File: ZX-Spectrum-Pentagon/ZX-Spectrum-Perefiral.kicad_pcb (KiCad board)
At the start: 2 copper layers, 4 parts, among them U1 74HC00

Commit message: add zxm_extrime_extension add 74XX283 to 74IEC start ZX-Spectrum-Perefiral project
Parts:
- removed C1: C, Capacitor_SMD:C_0805_2012Metric_Pad1.18x1.45mm_HandSolder
- removed R1, R2: R, Resistor_SMD:R_0805_2012Metric_Pad1.20x1.40mm_HandSolder
- removed U1: 74HC00, Package_SO:SOIC-14_3.9x8.7mm_P1.27mm
- added H1: MountingHole_Pad, MountingHole:MountingHole_3.2mm_M3_Pad_Via, F.Cu at (127.0, 24.1)
- added H2: MountingHole_Pad, MountingHole:MountingHole_3.2mm_M3_Pad_Via, F.Cu at (215.9, 39.4)
- added H3: MountingHole_Pad, MountingHole:MountingHole_3.2mm_M3_Pad_Via, F.Cu at (228.6, 64.8)
- added H4: MountingHole_Pad, MountingHole:MountingHole_3.2mm_M3_Pad_Via, F.Cu at (228.6, 144.8)
- added H5: MountingHole_Pad, MountingHole:MountingHole_3.2mm_M3_Pad_Via, F.Cu at (24.1, 144.8)
- added H6: MountingHole_Pad, MountingHole:MountingHole_3.2mm_M3_Pad_Via, F.Cu at (24.1, 64.8)
- added JCPU1: TOP LEVEL, ZX-Spectrum-Pentagon:PinSocket_2x30_P2.54mm_Vertical, F.Cu at (174.0, 33.0)
- added XMCPU1: EDGE-28M5, ZX-Spectrum-Pentagon:EDGE_28M5-2.54, F.Cu at (172.4, 24.1)
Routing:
- added copper zone on F.Cu, net GND
- added copper zone on B.Cu, net VCC
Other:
- board outline added: 213.1 x 129 mm
- board text added: "EDGE connector position X=172.44 Y=24.13 BOARD connector position X=173.99 Y=33.02 Hole1: X=127 Y=24.13, Hole2: X=215.9 Y=39.37 Hole3: X=228.6 Y=64.77, Hole4: X=228.6 Y=144.78 Hole5: X=24.13 Y=144.78, Hole6: X=24.13 Y=64.77"

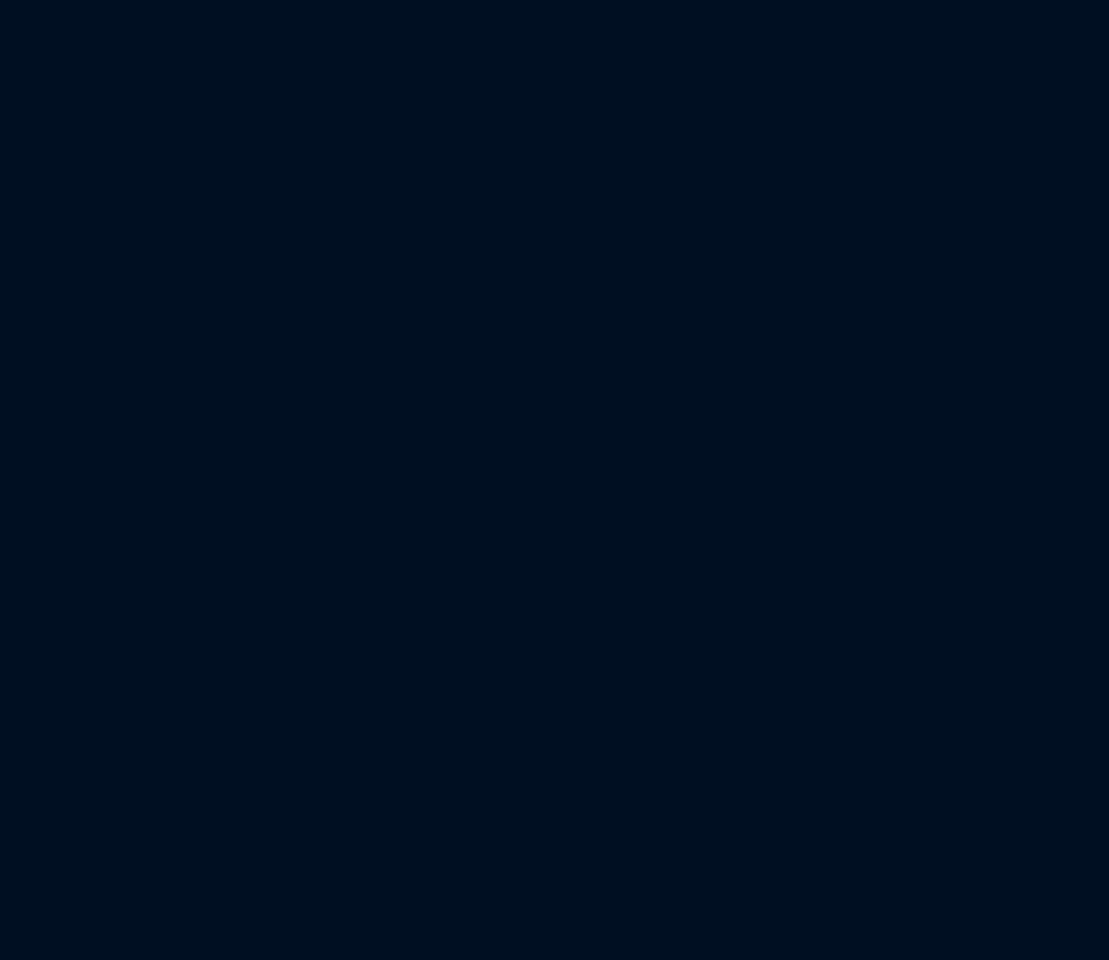
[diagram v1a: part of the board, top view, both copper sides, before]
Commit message: fix 74ICE, FDControlers, edge_lib library update all schematic and board fix ERC ZX-Spectrum-Perefiral
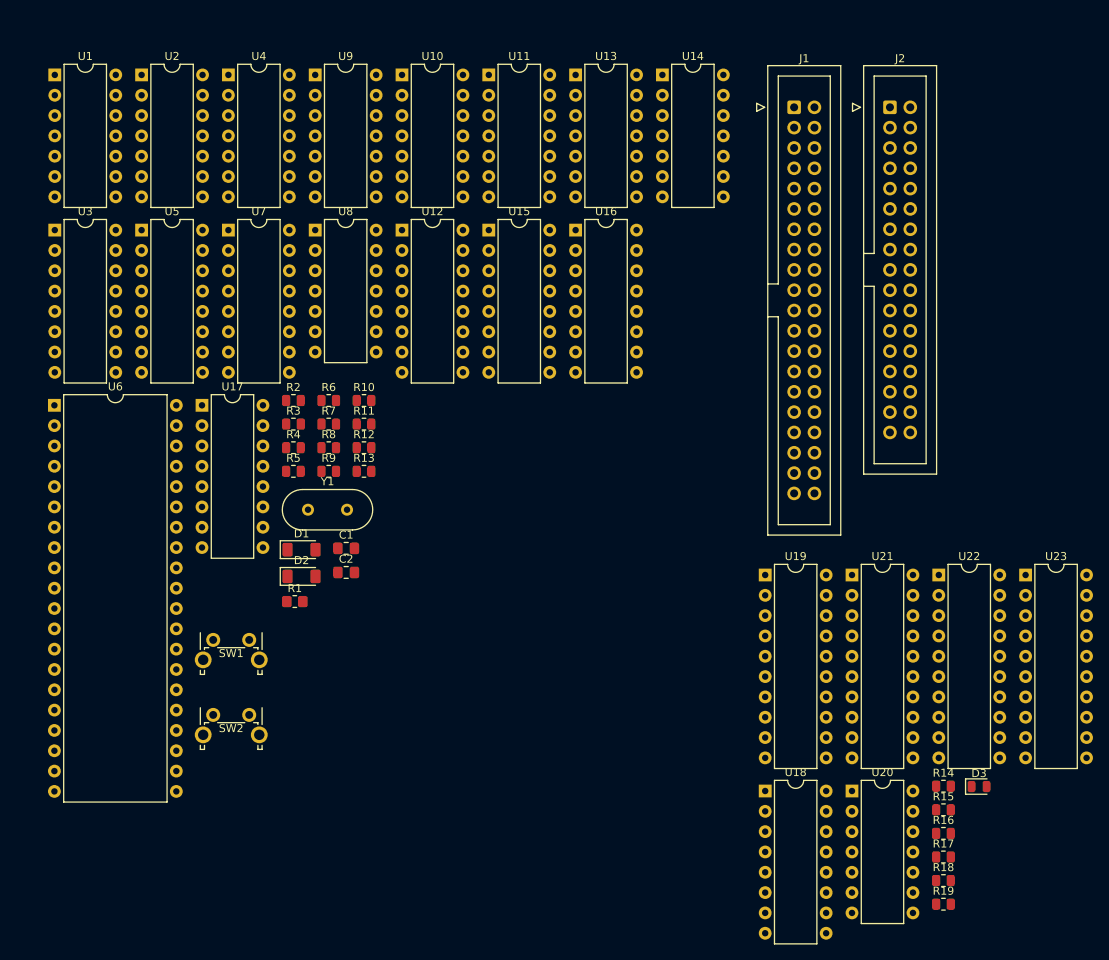
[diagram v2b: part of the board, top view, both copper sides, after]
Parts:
- added C1: 20pF, Capacitor_SMD:C_0805_2012Metric_Pad1.18x1.45mm_HandSolder, F.Cu at (284.6, 116.0)
- added C2: 20pF, Capacitor_SMD:C_0805_2012Metric_Pad1.18x1.45mm_HandSolder, F.Cu at (284.6, 119.1)
- added D1: 1N4148, Diode_SMD:D_MiniMELF, F.Cu at (279.1, 116.2)
- added D2: 1N4148, Diode_SMD:D_MiniMELF, F.Cu at (279.1, 119.6)
- added D3: RED, Diode_SMD:D_0805_2012Metric, F.Cu at (363.8, 145.8)
- added J1: IDE, Connector_IDC:IDC-Header_2x20_P2.54mm_Vertical, F.Cu at (340.6, 60.9)
- added J2: FDD, Connector_IDC:IDC-Header_2x17_P2.54mm_Vertical, F.Cu at (352.6, 60.9)
- added R1: 2MOm, Resistor_SMD:R_0805_2012Metric_Pad1.20x1.40mm_HandSolder, F.Cu at (278.2, 122.7)
- added R10: 10kOm, Resistor_SMD:R_0805_2012Metric, F.Cu at (286.9, 97.6)
- added R11: 10kOm, Resistor_SMD:R_0805_2012Metric, F.Cu at (286.9, 100.5)
- added R12: 10kOm, Resistor_SMD:R_0805_2012Metric, F.Cu at (286.9, 103.5)
- added R13: 10kOm, Resistor_SMD:R_0805_2012Metric, F.Cu at (286.9, 106.4)
- added R14: 10kOm, Resistor_SMD:R_0805_2012Metric, F.Cu at (359.3, 145.8)
- added R15: 10kOm, Resistor_SMD:R_0805_2012Metric, F.Cu at (359.3, 148.7)
- added R16: 10kOm, Resistor_SMD:R_0805_2012Metric, F.Cu at (359.3, 151.7)
- added R17: 10kOm, Resistor_SMD:R_0805_2012Metric, F.Cu at (359.3, 154.6)
- added R18: 10kOm, Resistor_SMD:R_0805_2012Metric, F.Cu at (359.3, 157.6)
- added R19: 10kOm, Resistor_SMD:R_0805_2012Metric, F.Cu at (359.3, 160.5)
- added R2: 10kOm, Resistor_SMD:R_0805_2012Metric, F.Cu at (278.1, 97.6)
- added R3: 10kOm, Resistor_SMD:R_0805_2012Metric, F.Cu at (278.1, 100.5)
- added R4: 1kOm, Resistor_SMD:R_0805_2012Metric, F.Cu at (278.1, 103.5)
- added R5: 1kOm, Resistor_SMD:R_0805_2012Metric, F.Cu at (278.1, 106.4)
- added R6: 1kOM, Resistor_SMD:R_0805_2012Metric, F.Cu at (282.5, 97.6)
- added R7: 1kOM, Resistor_SMD:R_0805_2012Metric, F.Cu at (282.5, 100.5)
- added R8: 1kOM, Resistor_SMD:R_0805_2012Metric, F.Cu at (282.5, 103.5)
- added R9: 10kOM, Resistor_SMD:R_0805_2012Metric, F.Cu at (282.5, 106.4)
- added SW1: MAGIC, Button_Switch_THT:SW_Tactile_SPST_Angled_PTS645Vx39-2LFS, F.Cu at (268.0, 127.5)
- added SW2: SOS/~{DOS}, Button_Switch_THT:SW_Tactile_SPST_Angled_PTS645Vx39-2LFS, F.Cu at (268.0, 136.9)
- added U1: 74HC04, Package_DIP:DIP-14_W7.62mm, F.Cu at (248.2, 56.9)
- added U10: 74HC03, Package_DIP:DIP-14_W7.62mm, F.Cu at (291.6, 56.9)
- added U11: 74HC74, Package_DIP:DIP-14_W7.62mm, F.Cu at (302.5, 56.9)
- added U12: 74HC166, Package_DIP:DIP-16_W7.62mm, F.Cu at (291.6, 76.3)
- added U13: 74HC30, Package_DIP:DIP-14_W7.62mm, F.Cu at (313.3, 56.9)
- added U14: 74HC32, Package_DIP:DIP-14_W7.62mm, F.Cu at (324.2, 56.9)
- added U15: 74HC175, Package_DIP:DIP-16_W7.62mm, F.Cu at (302.5, 76.3)
- added U16: 74HC161, Package_DIP:DIP-16_W7.62mm, F.Cu at (313.3, 76.3)
- added U17: 74HC283, Package_DIP:DIP-16_W7.62mm, F.Cu at (266.6, 98.2)
- added U18: 74HC138, Package_DIP:DIP-16_W7.62mm, F.Cu at (337.0, 146.4)
- added U19: 74HC245, Package_DIP:DIP-20_W7.62mm, F.Cu at (337.0, 119.4)
- added U2: 74HC74, Package_DIP:DIP-14_W7.62mm, F.Cu at (259.1, 56.9)
- added U20: 74HC32, Package_DIP:DIP-14_W7.62mm, F.Cu at (347.9, 146.4)
- added U21: 74HC574, Package_DIP:DIP-20_W7.62mm, F.Cu at (347.9, 119.4)
- added U22: 74HC244, Package_DIP:DIP-20_W7.62mm, F.Cu at (358.7, 119.4)
- added U23: 74HC574, Package_DIP:DIP-20_W7.62mm, F.Cu at (369.6, 119.4)
- added U3: 74HC138, Package_DIP:DIP-16_W7.62mm, F.Cu at (248.2, 76.3)
- added U4: 74HC05, Package_DIP:DIP-14_W7.62mm, F.Cu at (269.9, 56.9)
- added U5: 74HC367, Package_DIP:DIP-16_W7.62mm, F.Cu at (259.1, 76.3)
- added U6: FD1793, Package_DIP:DIP-40_W15.24mm, F.Cu at (248.2, 98.2)
- added U7: 74HC175, Package_DIP:DIP-16_W7.62mm, F.Cu at (269.9, 76.3)
- added U8: 74HC00, Package_DIP:DIP-14_W7.62mm, F.Cu at (280.8, 76.3)
- added U9: 74HC27, Package_DIP:DIP-14_W7.62mm, F.Cu at (280.8, 56.9)
- added Y1: 16MHz, Crystal:Crystal_HC49-U_Vertical, F.Cu at (279.9, 111.2)
- XMCPU1: footprint ZX-Spectrum-Pentagon:EDGE_28M5-2.54 -> edge:EDGE_28M5-2.54
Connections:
- net /Connectors/A0 renamed /A0
- net /Connectors/A1 renamed /A1
- net /Connectors/A10 renamed /A10
- net /Connectors/A11 renamed /A11
- net /Connectors/A12 renamed /A12
- net /Connectors/A13 renamed /A13
- net /Connectors/A14 renamed /A14
- net /Connectors/A15 renamed /A15
- net /Connectors/A2 renamed /A2
- net /Connectors/A3 renamed /A3
- net /Connectors/A4 renamed /A4
- net /Connectors/A5 renamed /A5
- net /Connectors/A6 renamed /A6
- net /Connectors/A7 renamed /A7
- net /Connectors/A8 renamed /A8
- net /Connectors/A9 renamed /A9
- net /Connectors/D0 renamed /D0
- net /Connectors/D1 renamed /D1
- net /Connectors/D2 renamed /D2
- net /Connectors/D3 renamed /D3
- net /Connectors/D4 renamed /D4
- net /Connectors/D5 renamed /D5
- net /Connectors/D6 renamed /D6
- net /Connectors/D7 renamed /D7
- net /Connectors/RA15 renamed /~{DOS}
- net /Connectors/~{IORQ} renamed /~{IORQ}
- net /Connectors/~{M1} renamed /~{M1}
- net /Connectors/~{MREQ} renamed /~{MREQ}
- net /Connectors/~{NMI} renamed /~{NMI}
- net /Connectors/~{RD} renamed /~{RD}
- net /Connectors/~{RESET} renamed /~{RESET}
- net /Connectors/~{WR} renamed /~{WR}
- JCPU1 pad 31: unconnected-(JCPU1-Pin_31-Pad31) -> /~{ZX128}
- XMCPU1 pad A16: unconnected-(XMCPU1-PadA16) -> /~{ZX128}

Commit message: FDControlers rename from VCC1 to VDD zx_custom_symbol add connector Conn_02x32_Odd_Even ZX-Spectrum-Pentagon rename from +9V to POWER ZX-Spectrum-Perefiral improve schematic
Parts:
- removed the D1 at (279.1, 116.2)
- removed JCPU1: TOP LEVEL, ZX-Spectrum-Pentagon:PinSocket_2x30_P2.54mm_Vertical
- added CPS1: 47uF/16V, Capacitor_Tantalum_SMD:CP_EIA-3216-18_Kemet-A_Pad1.58x1.35mm_HandSolder, F.Cu at (370.7, -26.0)
- added CPS2: 330uF/50V, Capacitor_Tantalum_SMD:CP_EIA-7343-31_Kemet-D_Pad2.25x2.55mm_HandSolder, F.Cu at (364.3, -36.4)
- added CPS3: 100nF, Capacitor_SMD:C_0805_2012Metric_Pad1.18x1.45mm_HandSolder, F.Cu at (371.8, -37.8)
- added CPS4: 330uF/50V, Capacitor_Tantalum_SMD:CP_EIA-7343-31_Kemet-D_Pad2.25x2.55mm_HandSolder, F.Cu at (364.3, -30.5)
- added CPS5: 100nF, Capacitor_SMD:C_0805_2012Metric_Pad1.18x1.45mm_HandSolder, F.Cu at (371.8, -34.8)
- added CPS6: 4,7uF/16V, Capacitor_Tantalum_SMD:CP_EIA-3216-18_Kemet-A_Pad1.58x1.35mm_HandSolder, F.Cu at (370.7, -22.9)
- added CPS7: 330pF, Capacitor_SMD:C_0805_2012Metric_Pad1.18x1.45mm_HandSolder, F.Cu at (371.8, -31.8)
- added D3: 1N4148, Diode_SMD:D_MiniMELF, F.Cu at (282.3, 131.2)
- added DPS1: 1N5819, Diode_SMD:D_SOD-323_HandSoldering, F.Cu at (347.0, -23.6)
- added DPS2: SS34, Diode_SMD:D_SMA, F.Cu at (370.9, -42.5)
- added J1: Conn_02x32_Odd_Even, Connector_PinSocket_2.54mm:PinSocket_2x32_P2.54mm_Vertical, F.Cu at (132.1, 31.8)
- added LPS1: 33uH, Inductor_SMD:L_12x12mm_H6mm, F.Cu at (351.8, -32.2)
- added LPS2: 220uH, CDInductor:CD43, F.Cu at (370.0, -48.2)
- added RPS1: 1, Resistor_SMD:R_0805_2012Metric_Pad1.20x1.40mm_HandSolder, F.Cu at (364.5, -50.2)
- added RPS2: 13kOm, Resistor_SMD:R_0805_2012Metric_Pad1.20x1.40mm_HandSolder, F.Cu at (364.5, -47.2)
- added RPS3: 180, Resistor_SMD:R_0805_2012Metric_Pad1.20x1.40mm_HandSolder, F.Cu at (364.5, -44.3)
- added RPS4: 1,5kOm, Resistor_SMD:R_0805_2012Metric_Pad1.20x1.40mm_HandSolder, F.Cu at (364.5, -41.3)
- added UPS1: LM2596S-5.0V, Package_TO_SOT_SMD:TO-263-5_TabPin3, F.Cu at (355.1, -45.5)
- added UPS2: MC34063A, Package_SO:SO-8_3.9x4.9mm_P1.27mm, F.Cu at (363.4, -24.2)
- SW2: value SOS/~{DOS} -> ~{SOS}/DOS
- moved D2 8.92 mm to (282.3, 127.9)
- moved U14 5.39 mm to (318.8, 56.9)
- moved U16 4.71 mm to (308.6, 76.2)
- moved U13 4.71 mm to (308.6, 56.9)
- moved U15 4.02 mm to (298.4, 76.2)
- moved U10 4.02 mm to (298.4, 56.9)
- moved U12 3.33 mm to (288.3, 76.2)
- moved U8 3.33 mm to (288.3, 56.9)
- moved U11 2.64 mm to (278.1, 76.2)
- moved U9 2.64 mm to (278.1, 56.9)
- moved U4 1.95 mm to (268.0, 56.9)
- moved U7 1.94 mm to (268.0, 76.2)
- moved U5 1.26 mm to (257.8, 76.2)
- moved U2 1.26 mm to (257.8, 56.9)
- moved U17 1.25 mm to (265.4, 97.8)
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- renumbered D3 to D1, J1 to J2, J2 to J3, R7 to R1, R1 to R2, R2 to R3, R3 to R4, R4 to R5, R5 to R6, R6 to R7, U11 to U10, U8 to U11, U10 to U8
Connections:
- D2 pad 1: GND -> VDD
- D2 pad 2: /+12 -> +12V
- R1 pad 2: Net-(U10C-~{Y}) -> /FDC/~{CSWG}
- U11 pad 1: /FDC/~{CEA} -> Net-(U11A-A)
- U11 pad 2: /FDC/~{CEB} -> Net-(U11A-A)
- U11 pad 3: /FDC/~{CSWG} -> Net-(U11A-~{Y})
- U12 pad 13: Net-(U10C-A) -> Net-(U11A-A)
- U2 pad 8: unconnected-(U2B-~{Q}-Pad8) -> Net-(U2B-~{Q})
- U4 pad 13: Net-(U10C-~{Y}) -> Net-(U11A-~{Y})
- U6 pad 40: GND -> VDD
- U8 pad 10: Net-(U10C-A) -> /FDC/~{CEB}
- U8 pad 8: Net-(U10C-~{Y}) -> /FDC/~{CSWG}
- U8 pad 9: Net-(U10C-A) -> /FDC/~{CEA}
- U9 pad 1: /~{NMI} -> Net-(U2B-~{Q})
- U9 pad 2: /FDC/~{SOS}/DOS -> Net-(U2B-~{Q})
- XMCPU1 pad A25: /Connectors/~{ROMSEL} -> /Connectors/~{CSROM}
- XMCPU1 pad A4: /Connectors/+9V -> /Connectors/F
